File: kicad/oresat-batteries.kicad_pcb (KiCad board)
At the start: 4 copper layers, 99.8 x 94.6 mm, 319 parts, among them J1 J-SAMTEC-TFM-120-X1-XXX-D-RA, J2 SM14B-SHLS-TF, Q1 DMP2240UDM-7, Q10 SI7111EDN-T1-GE3, Q11 SI7111EDN-T1-GE3, Q12 SI7111EDN-T1-GE3, Q13 SI7111EDN-T1-GE3, Q14 NTR4101, Q15 NTR4101, Q16 SI7111EDN-T1-GE3, Q17 SI7111EDN-T1-GE3, Q18 SI7111EDN-T1-GE3, Q19 SI7111EDN-T1-GE3, Q2 PMV45ENR, Q20 PMV45ENR, Q21 PMV45ENR, Q22 SQS484ENW-T1_GE3, Q24 PMV45ENR, Q25 PMV45ENR, Q26 PMV45ENR, Q27 PMV45ENR, Q29 SQS484ENW-T1_GE3, Q3 DMP3050LVTQ-7, Q30 SI7111EDN-T1-GE3, Q31 SI7111EDN-T1-GE3, Q32 NTR4101, Q33 NTR4101, Q34 SI7111EDN-T1-GE3, Q35 SI7111EDN-T1-GE3, Q36 SI7111EDN-T1-GE3, Q37 SI7111EDN-T1-GE3, Q38 PMV45ENR, Q39 PMV45ENR, Q4 DMP3050LVTQ-7, Q42 DMP2240UDM-7, Q43 DMP2240UDM-7, Q44 PMV45ENR, Q5 PMV45ENR, Q6 PMV45ENR, Q7 PMV45ENR, Q8 PMV45ENR, Q9 PMV45ENR, SW1 Omron D2F-L3-D (LEFT), SW2 Omron D2F-L3-D (RIGHT), SW3 OMRON D2F-L3-D (LEFT), SW4 OMRON D2F-L3-D (RIGHT), U1 MAX7310, U10 LTC4412, U11 LTC4412, U12 MAX17205G, U13 S-8209AAA-T8T1U, U14 S-8209AAA-T8T1U, U15 LTC4412, U16 LTC4412, U17 MAX17205G, U2 MIC842LYC5, U20 TCAN330, U21 STM32F091C, U3 MIC842LYC5, U4 MAX4211, U5 TPS6211X, U6 TS5A21366DCUR, U8 S-8209AAA-T8T1U, U9 S-8209AAA-T8T1U, X3 ECS-160-10-36Q-ES-TR

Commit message: Routing complete!
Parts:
- moved C14 47.5 mm to (139.8, 70.2)
- moved C12 45.0 mm to (138.2, 82.1), turned to -90 degrees
- moved C13 44.7 mm to (137.8, 85.2)
- moved R87 44.5 mm to (137.8, 84.1), turned to 180 degrees
- moved C37 42.8 mm to (135.3, 74.0), turned to -90 degrees
- moved U2 0.95 mm to (139.9, 68.7)
- moved R22 0.78 mm to (134.2, 74.0), turned to 90 degrees
- moved R37 0.37 mm to (137.1, 82.1)
- moved TP6 0.14 mm to (142.0, 68.4)
- turned D3 to 90 degrees
- turned R3 to 0 degrees
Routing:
- net /Battery Pack 2 (TOP)/INTERCELL-PK2: track 127.1 -> 134.1 mm
- net VBUSP: track 126.9 -> 129.2 mm, vias 13 -> 14
- net Net-(U2-INP): track 4.84 -> 6.72 mm
- net /Power/CB_CTRL: track 29.9 -> 31.6 mm
- net Net-(D3-A): track 0.00 -> 1.22 mm
- net (no net): track 1.22 -> 0.00 mm
- net Net-(C13-Pad2): track 0.00 -> 1.10 mm
- net VPD: track 74.8 -> 75.6 mm
- net Net-(U2-OUT): track 4.37 -> 4.96 mm, vias 0 -> 1
- net GND: vias 279 -> 276

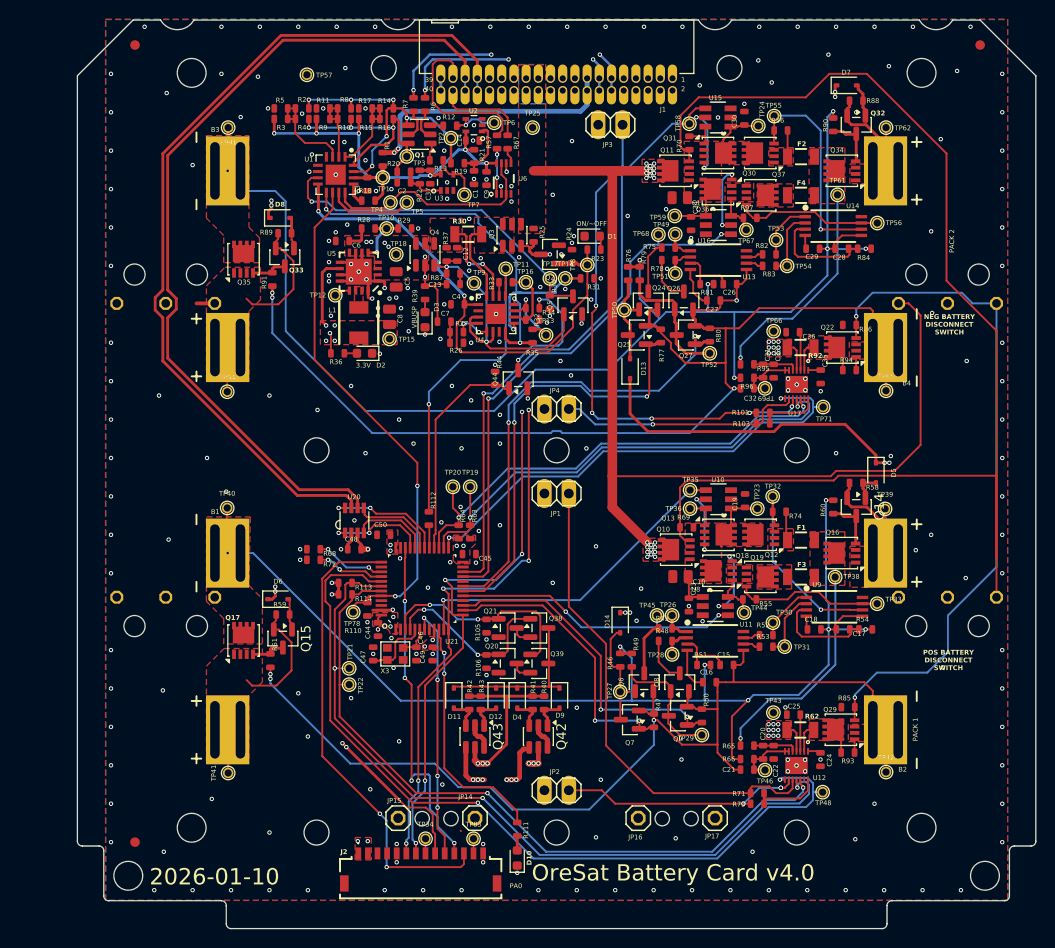
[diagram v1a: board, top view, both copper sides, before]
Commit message: Updated BOM, ready for polish and switch to MCXN
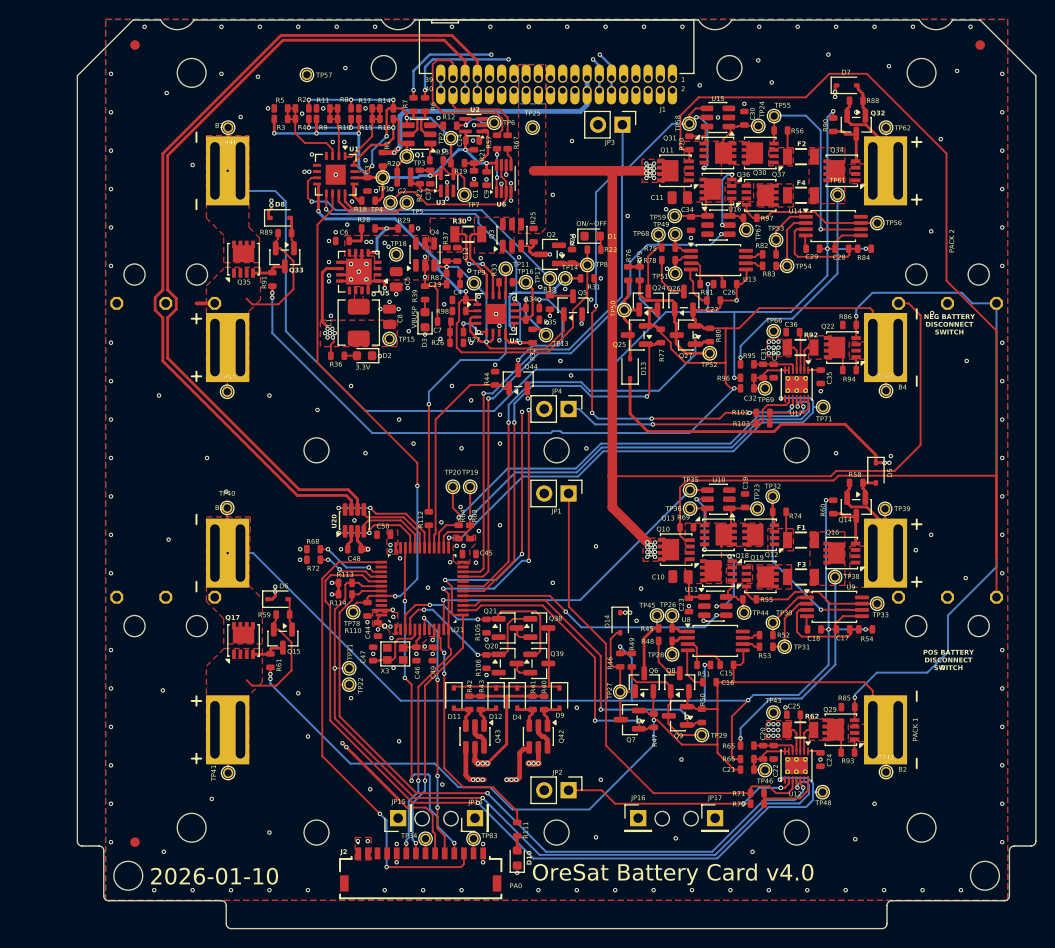
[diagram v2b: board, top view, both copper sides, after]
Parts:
- removed TP10, TP12: TEST-POINT-LARGE-SQUARE, oresat-misc:TestPoint-0.75mm-th
- added R98: 10k, oresat-passives:0603-C-NOSILK, F.Cu at (138.3, 88.0)
- B1, B2, B3, B4: footprint oresat-batteries:18650 -> oresat-misc:18650
- JP1, JP2, JP3, JP4: footprint oresat-batteries:1X02 -> Connector_PinHeader_2.54mm:PinHeader_1x02_P2.54mm_Vertical
- JP14, JP15, JP16, JP17: footprint oresat-batteries:1X01 -> Connector_PinHeader_2.54mm:PinHeader_1x01_P2.54mm_Vertical
- L1: footprint oresat-batteries:ECS-MPI4040 -> oresat-passives:L_ECS-MPI4040
- U1, U4: footprint oresat-batteries:QFN65P400X400X80-17T210 -> Package_DFN_QFN:QFN-16-1EP_4x4mm_P0.65mm_EP2.1x2.1mm
- U10, U11, U15, U16: footprint oresat-batteries:SOT23-6 -> Package_TO_SOT_SMD:TSOT-23-6
- U12, U17: footprint oresat-batteries:21-0137I_T1433-2 -> Package_DFN_QFN:TDFN-14-1EP_3x3mm_P0.4mm_EP1.78x2.35mm_ThermalVias
- U13, U14, U8, U9: footprint oresat-batteries:TSSOP8 -> Package_SO:TSSOP-8_4.4x3mm_P0.65mm
- U2, U3: footprint oresat-batteries:SC70-5 -> Package_TO_SOT_SMD:SOT-353_SC-70-5
- U20: footprint oresat-batteries:SOT23-8_TI-DCN -> Package_TO_SOT_SMD:SOT-23-8
- U5: value TPS6211X -> TPS62111RSA; footprint oresat-batteries:S-PVQFN-16 -> Package_DFN_QFN:Texas_RSA_VQFN-16-1EP_4x4mm_P0.65mm_EP2.7x2.7mm
- U6: footprint oresat-batteries:DCU0008A_N -> Package_SO:VSSOP-8_2.3x2mm_P0.5mm
- moved JP1 1.25 mm to (149.8, 107.0), turned to -90 degrees
- moved JP2 1.25 mm to (149.8, 137.9), turned to -90 degrees
- moved JP3 1.25 mm to (155.3, 68.6), turned to -90 degrees
- moved JP4 1.25 mm to (149.8, 98.2), turned to -90 degrees
- moved C4 0.48 mm to (138.3, 86.8)
- moved D2 0.25 mm to (128.5, 92.7)
- moved R36 0.25 mm to (125.7, 92.7)
- turned L1 to -90 degrees
- turned U10 to 180 degrees
- turned U11 to 0 degrees
- turned U15 to 180 degrees
- turned U16 to 0 degrees
- turned U2 to 180 degrees
- turned U20 to 90 degrees
- turned U3 to 90 degrees
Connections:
- U2 pad 3: (no net) -> unconnected-(U2-Pad3)
- U3 pad 3: (no net) -> unconnected-(U3-Pad3)
- U4 pad 2: (no net) -> Net-(U4-IN)
- U5 pad 13: Net-(U5-PG) -> unconnected-(U5-PG-Pad13)
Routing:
- net Net-(U5-PG): track 1.67 -> 0.00 mm
- net Net-(U4-IN): track 0.00 -> 1.21 mm
- net GND: track 29.5 -> 28.3 mm, vias 276 -> 267
- net /Power/ON/~{OFF}: track 54.5 -> 55.3 mm
- net 3.3V: track 33.7 -> 34.0 mm, vias 18 -> 20
- net Net-(U5-SYNC): vias 1 -> 2
